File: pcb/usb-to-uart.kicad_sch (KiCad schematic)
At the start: 8 parts, among them Q1 MUN5211DW1, U2 CP2102N-Axx-xQFN24

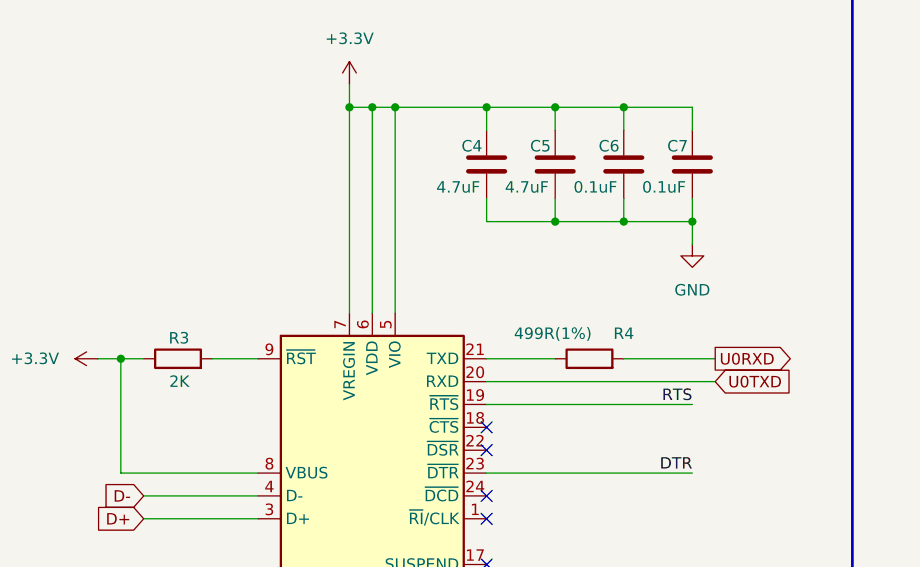
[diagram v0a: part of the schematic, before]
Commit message: ADD new picture, and propper GND plane on top layer
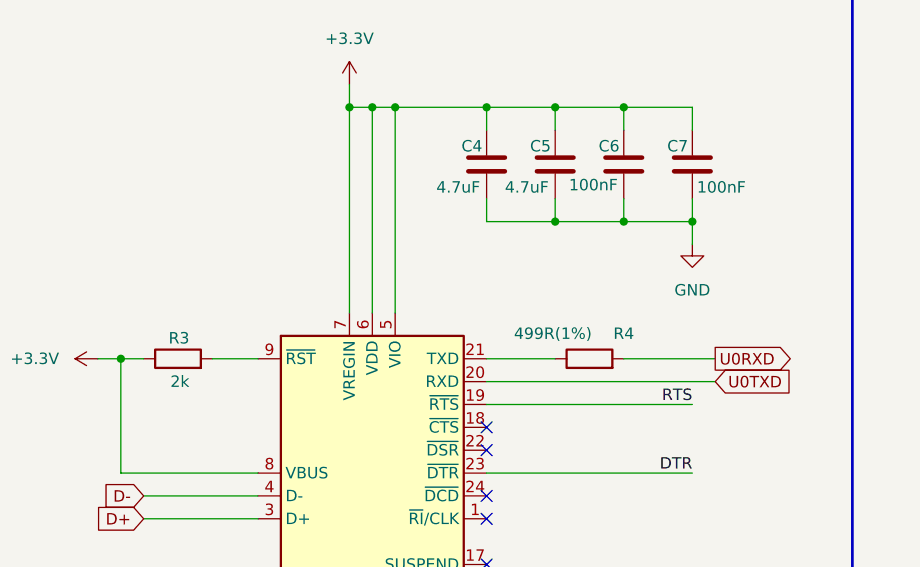
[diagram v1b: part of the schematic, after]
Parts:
- C6, C7: value 0.1uF -> 100nF
- R3: value 2K -> 2k
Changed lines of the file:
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@@
       (effects (font (size 1.27 1.27)) (justify left))
     )
-    (property "Value" "2K" (id 1) (at 76.2 88.9 90)
+    (property "Value" "2k" (id 1) (at 76.2 88.9 90)
       (effects (font (size 1.27 1.27)) (justify left))
     )
@@
       (effects (font (size 1.27 1.27)) (justify left))
     )
-    (property "Value" "0.1uF" (id 1) (at 126.492 67.31 0)
+    (property "Value" "100nF" (id 1) (at 132.588 67.31 0)
       (effects (font (size 1.27 1.27)) (justify left))
     )
@@
       (effects (font (size 1.27 1.27)) (justify left))
     )
-    (property "Value" "0.1uF" (id 1) (at 118.872 67.31 0)
-      (effects (font (size 1.27 1.27)) (justify left))
-    )
+    (property "Value" "100nF" (id 1) (at 118.364 67.056 0)
+      (effects (font (size 1.27 1.27)) (justify left))
+    )

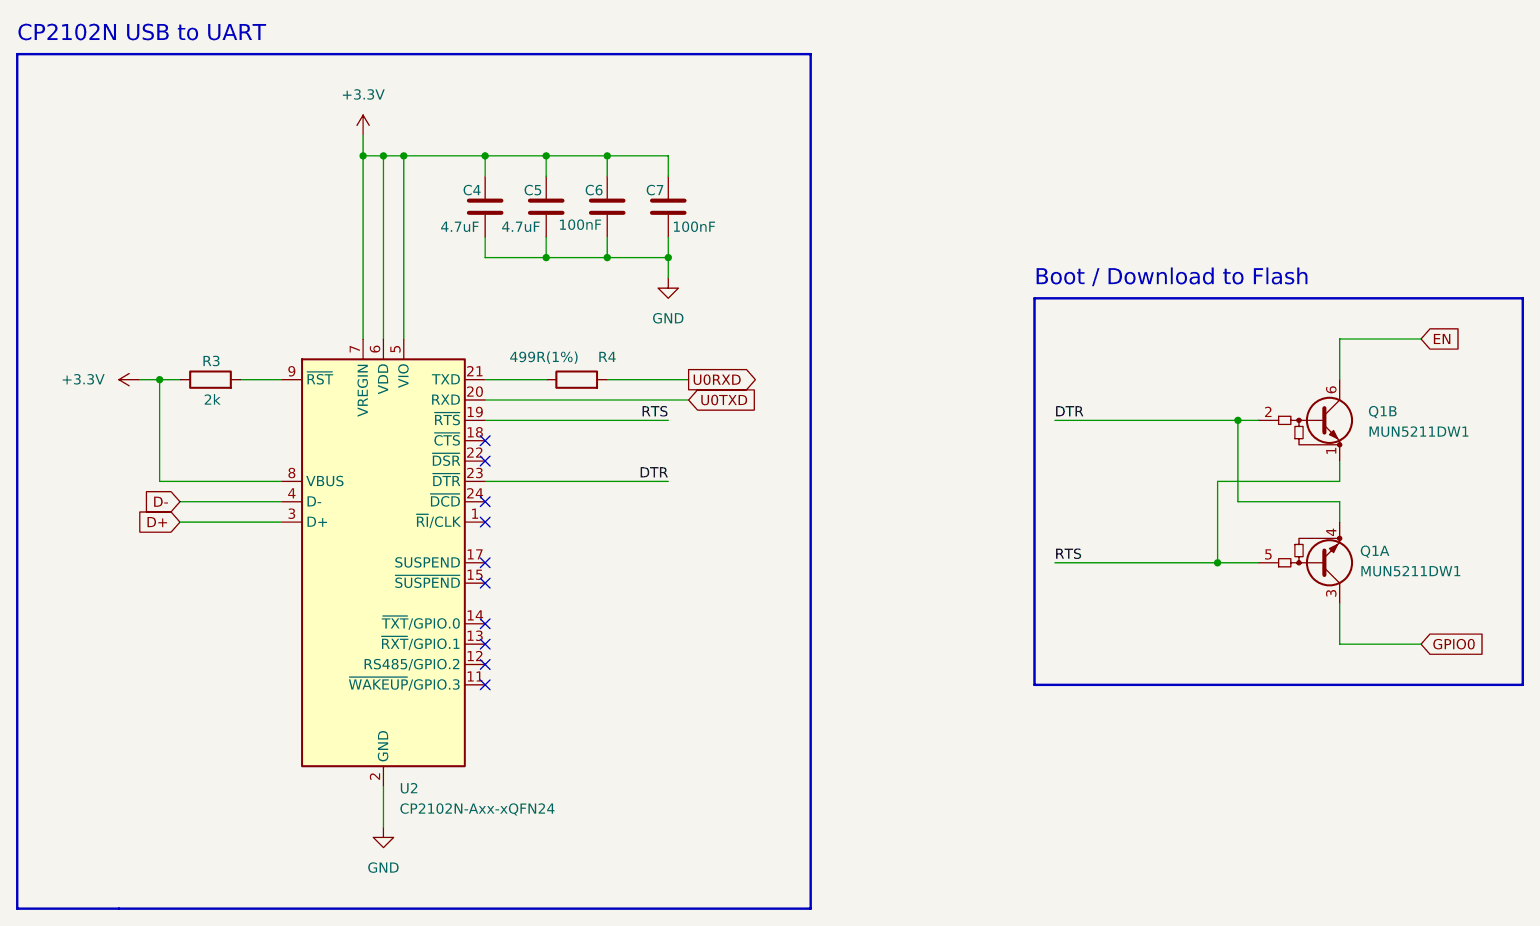
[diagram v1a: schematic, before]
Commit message: REF PCB Layout, Switch to new USB-C Receptable
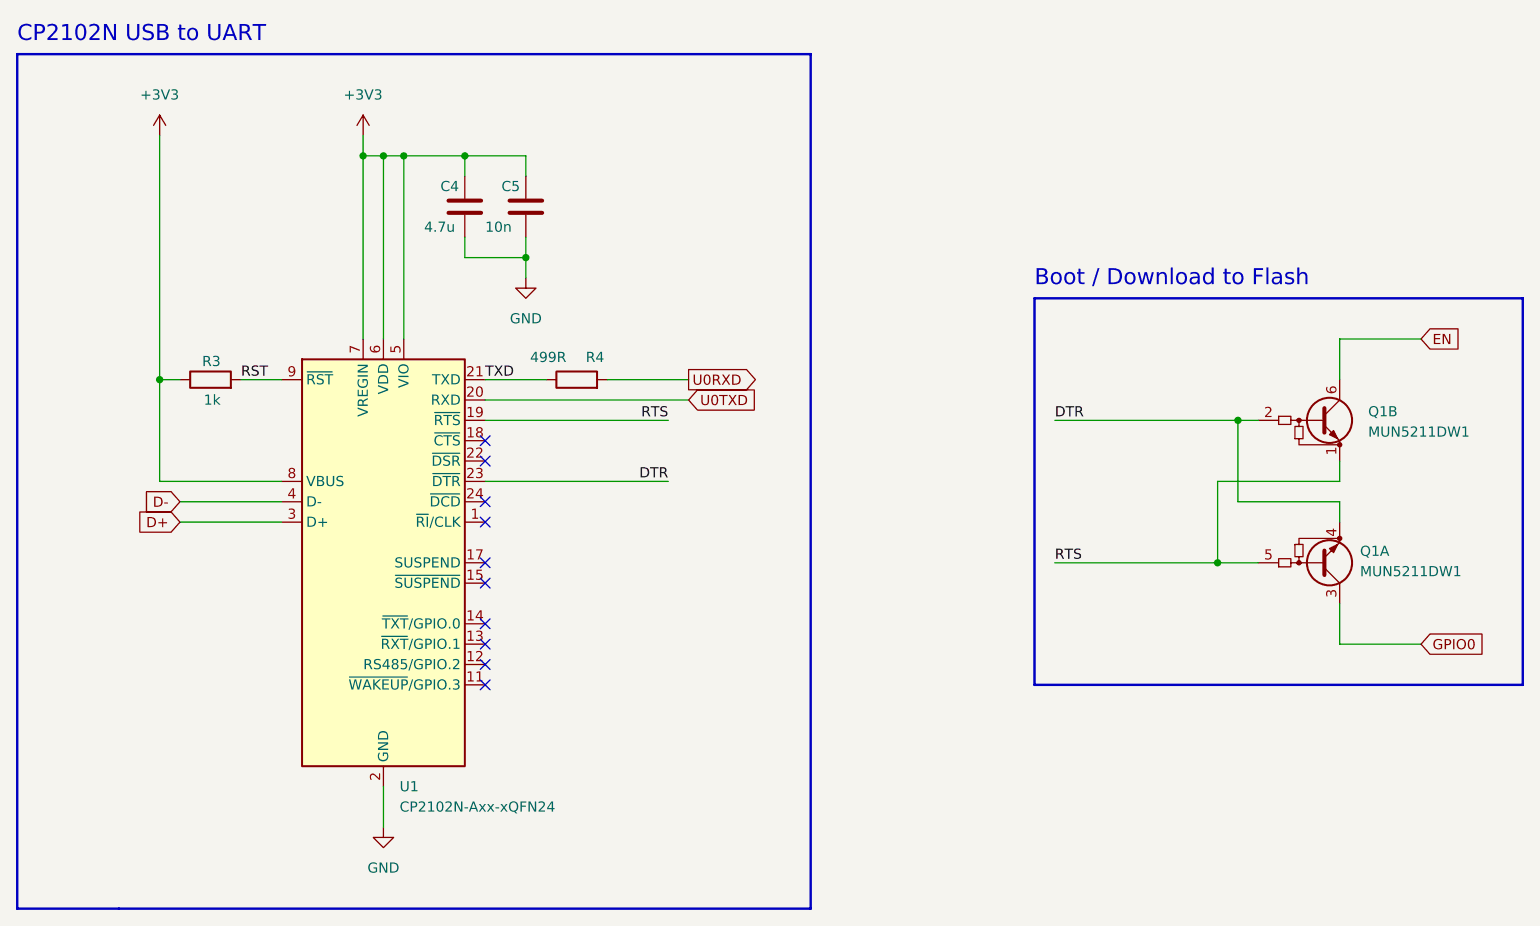
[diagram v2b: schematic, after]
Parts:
- removed C4: 4.7uF, Capacitor_SMD:C_0402_1005Metric, symbol Device:C
- removed C7: 100nF, Capacitor_SMD:C_0402_1005Metric, symbol Device:C
- C4: renamed from C5; value 4.7uF -> 4.7u
- C5: renamed from C6; value 100nF -> 10n
- R3: value 2k -> 1k
- R4: value 499R(1%) -> 499R
- renumbered U2 to U1
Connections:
- net RST: now reaches R3.2, U1.9 (~{RST})
- net TXD: now reaches R4.1, U1.21 (TXD)
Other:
- moved on the sheet: C4, C5
